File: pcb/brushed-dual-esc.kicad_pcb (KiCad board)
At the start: 2 copper layers, 29.5 x 25 mm, 33 parts, among them J1 XT30PW-M, J2 TC2030-NL, J3 Conn_02x03_Odd_Even, J4 XT30PW-F, J5 XT30PW-F, U1 AZ1117-5.0, U2 TLV77133PDBVR, U3 STM32C011F4Ux, U4 DRV8231ADSGR, U5 DRV8231ADSGR

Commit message: Start layout
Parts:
- removed D1: B1911USD, LED_SMD:LED_0603_1608Metric
- removed G***: LOGO, LOGO
- removed J1: XT30PW-M, Connector_AMASS:AMASS_XT30PW-M_1x02_P2.50mm_Horizontal
- removed R1: 270, Resistor_SMD:R_0603_1608Metric
- removed TP1: 5V, TestPoint:TestPoint_Pad_D2.0mm
- removed TP2: 3V3, TestPoint:TestPoint_Pad_D1.5mm
- removed U4, U5: DRV8231ADSGR, Package_SON:WSON-8-1EP_2x2mm_P0.5mm_EP0.9x1.6mm
- removed kibuzzard-68AF2469 (x2): G***, kibuzzard-68AF2469
- added D2: B1911USD, LED_SMD:LED_0603_1608Metric, F.Cu at (109.3, 106.0)
- added H1: M2, MountingHole:MountingHole_2.2mm_M2, F.Cu at (147.5, 52.5)
- added H2: M2, MountingHole:MountingHole_2.2mm_M2, F.Cu at (172.5, 72.5)
- added J6: DRV2_OUT1, Connector_Wire:SolderWirePad_1x01_SMD_2x4mm, F.Cu at (151.5, 72.5)
- added J7: DRV2_OUT2, Connector_Wire:SolderWirePad_1x01_SMD_2x4mm, F.Cu at (154.5, 72.5)
- added J8: +BATT, Connector_Wire:SolderWirePad_1x01_SMD_2x4mm, F.Cu at (172.5, 54.5)
- added J9: -BATT, Connector_Wire:SolderWirePad_1x01_SMD_2x4mm, F.Cu at (172.5, 59.5)
- added R6: 270, Resistor_SMD:R_0603_1608Metric, F.Cu at (106.0, 106.0)
- added U6: DRV8231ADDAR, Package_SO:Texas_HSOP-8-1EP_3.9x4.9mm_P1.27mm, F.Cu at (166.0, 66.0)
- added U7: DRV8231ADDAR, Package_SO:Texas_HSOP-8-1EP_3.9x4.9mm_P1.27mm, F.Cu at (153.0, 66.0)
- C1, C3: value 22u 16V -> CL21A226KOQNNNG; footprint Capacitor_SMD:C_0805_2012Metric -> Capacitor_SMD:C_1206_3216Metric
- C5: value ESS107M016AC2KA -> A750EM337M1CAAE015; footprint Capacitor_THT:CP_Radial_D5.0mm_P2.00mm -> Capacitor_THT:C_Radial_D6.3mm_H11.0mm_P2.50mm; moved to F.Cu
- J3: value Conn_02x03_Odd_Even -> DRV1_OUT1; footprint Connector_PinHeader_2.54mm:PinHeader_2x03_P2.54mm_Horizontal -> Connector_Wire:SolderWirePad_1x01_SMD_2x4mm; moved to F.Cu
- J4: value XT30PW-F -> Conn_01x04_Pin; footprint Connector_AMASS:AMASS_XT30PW-F_1x02_P2.50mm_Horizontal -> Connector_PinHeader_2.54mm:PinHeader_1x04_P2.54mm_Vertical; moved to F.Cu
- J5: value XT30PW-F -> DRV1_OUT2; footprint Connector_AMASS:AMASS_XT30PW-F_1x02_P2.50mm_Horizontal -> Connector_Wire:SolderWirePad_1x01_SMD_2x4mm; moved to F.Cu
- R2: value 30k -> 47k
- U1: value AZ1117-5.0 -> AZ1117CH-5.0TRG1
- U3: value STM32C011F4Ux -> STM32C011F6U6
- moved R4 49.0 mm to (173.3, 90.9), turned to 0 degrees
- moved C5 46.6 mm to (133.8, 142.5)
- moved C1 45.9 mm to (171.0, 51.5)
- moved J4 42.6 mm to (147.5, 57.7)
- moved C9 41.2 mm to (169.3, 88.4), turned to 0 degrees
- moved J3 40.7 mm to (164.5, 72.5), turned to 0 degrees
- moved R5 39.5 mm to (155.0, 60.5)
- moved C11 38.8 mm to (169.3, 93.4), turned to 0 degrees
- moved R3 38.6 mm to (96.1, 77.8)
- moved R2 37.8 mm to (96.2, 80.5), turned to 0 degrees
- moved C4 36.6 mm to (153.5, 52.0)
- moved U2 36.3 mm to (156.5, 52.0)
- moved C2 35.9 mm to (159.5, 52.0)
- moved C3 35.1 mm to (165.0, 51.5), turned to 0 degrees
- moved J5 34.6 mm to (167.5, 72.5)
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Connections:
- J3 pad 1: /RX_CH2 -> /DRV1_OUT1
- J4 pad 1: /DRV1_OUT2 -> /RX_CH2
- J4 pad 2: /DRV1_OUT1 -> /RX_CH1
- J5 pad 1: /DRV2_OUT2 -> /DRV1_OUT2
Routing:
- net +3V3: track 73.9 -> 0.00 mm, vias 2 -> 0
- net /DRV2_IN1: track 21.6 -> 0.00 mm, vias 4 -> 0
- net /DRV1_IN1: track 20.6 -> 0.00 mm, vias 2 -> 0
- net /DRV1_IN2: track 20.0 -> 0.00 mm
- net /DRV2_IN2: track 19.8 -> 0.00 mm, vias 4 -> 0
- net /DRV2_ISENSE: track 18.9 -> 0.00 mm, vias 4 -> 0
- net /DRV1_ISENSE: track 15.7 -> 0.00 mm, vias 2 -> 0
- net /RX_CH1: track 12.7 -> 0.00 mm, vias 1 -> 0
- net /RX_CH2: track 11.1 -> 0.00 mm, vias 1 -> 0
- net /~{RESET}: track 11.1 -> 0.00 mm, vias 4 -> 0
- net GND: track 8.17 -> 0.00 mm, vias 36 -> 0
- net /SWDIO: track 4.36 -> 0.00 mm
- net /BATT_SENSE: track 4.25 -> 0.00 mm
- net /SWCLK: track 4.05 -> 0.00 mm
- net Net-(D1-A): track 2.58 -> 0.00 mm
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- removed copper zone on F.Cu, net +3V3
- removed copper zone on F.Cu, net +5V
- removed copper zone on F.Cu, net +BATT
- removed copper zone on F.Cu, net /DRV1_OUT1
- removed copper zone on F.Cu, net /DRV1_OUT2
- removed copper zone on F.Cu, net /DRV2_OUT1
- removed copper zone on F.Cu, net /DRV2_OUT2
- removed copper zone on B.Cu, net GND
- removed copper zone on F.Cu, net GND
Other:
- board size 29.5 x 25 mm -> 30 x 25 mm
- board text removed: "3V3"
- board text removed: "5V 1A"
- board text removed: "CH1"
- board text removed: "CH2"
- board text removed: "Clarkson"
- board text removed: "Combat Robotics"
- board text removed: "Designed by Sigmond Kukla in 2025"
- board text removed: "GND"
- board text removed: "JLCJLCJLCJLC"
- board text removed: "SIG"
- board text removed: "University"

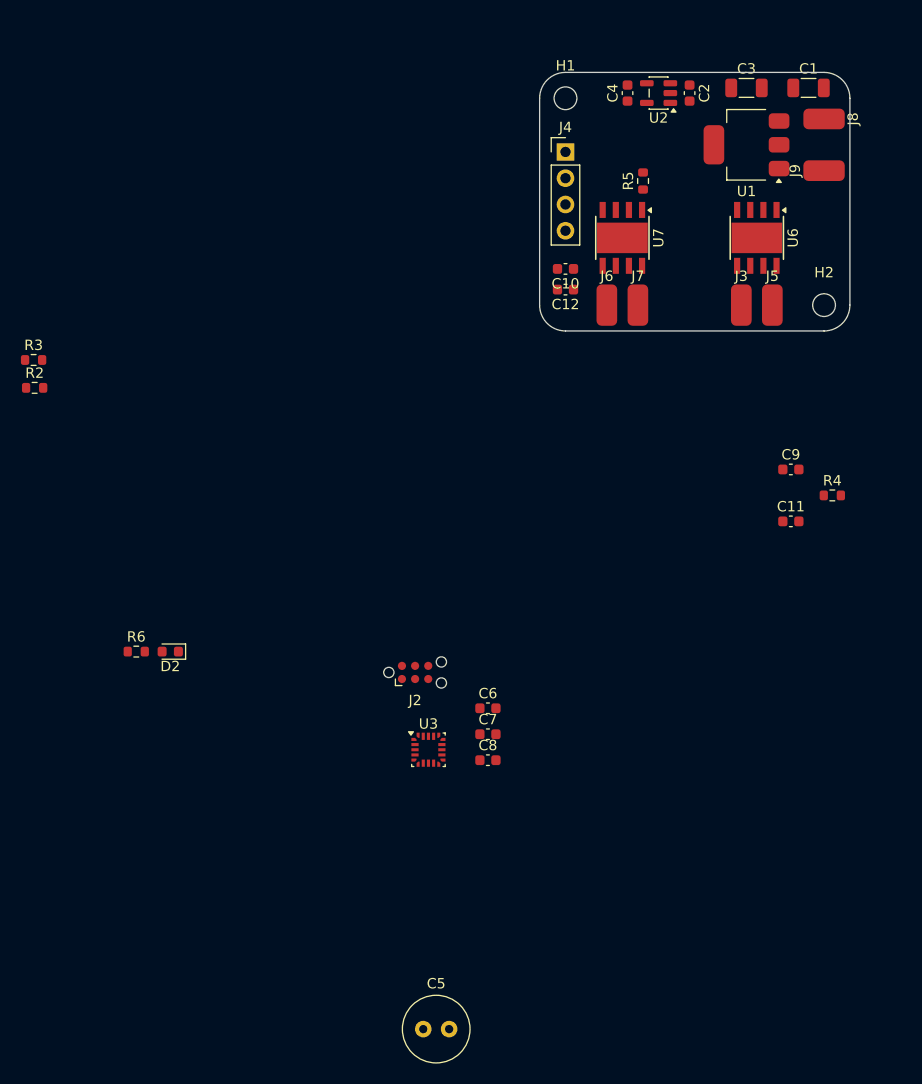
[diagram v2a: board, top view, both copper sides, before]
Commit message: Fit everything on the board
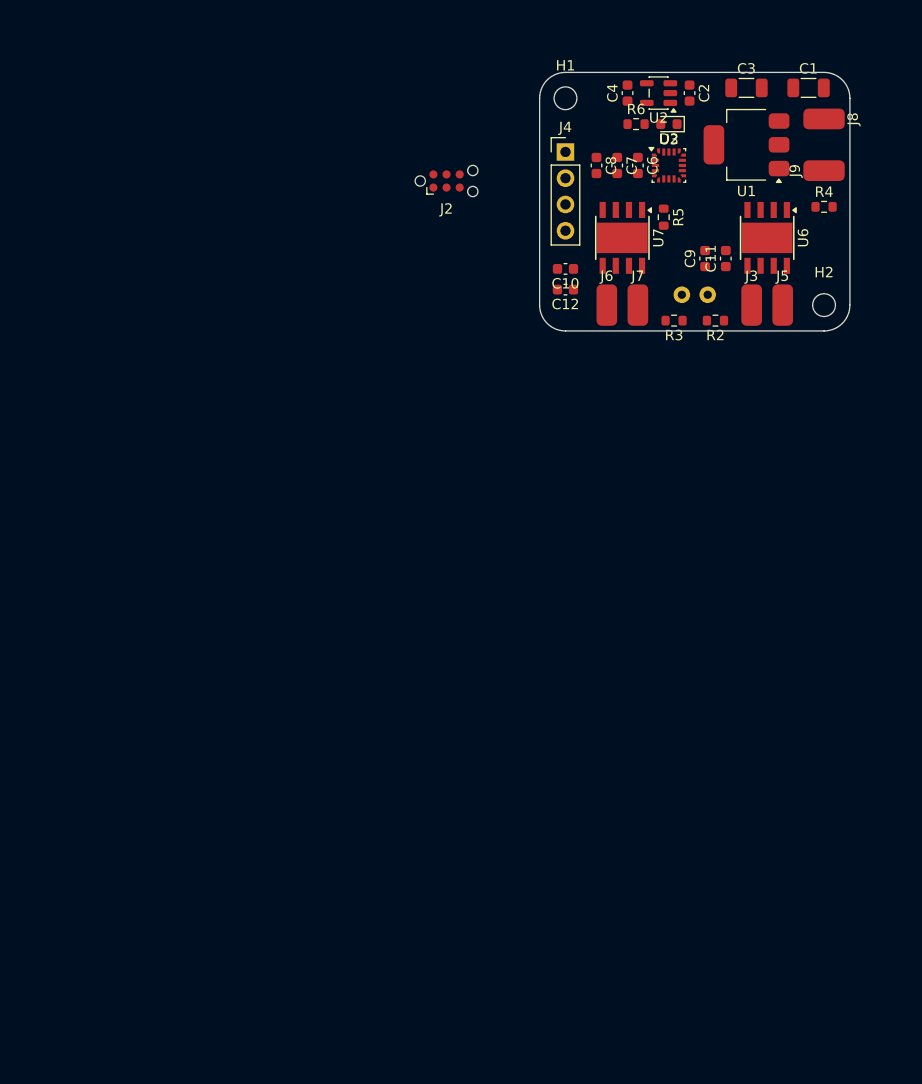
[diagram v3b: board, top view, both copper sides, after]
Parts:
- C5: moved to B.Cu
- moved C5 76.1 mm to (161.2, 71.5), turned to 180 degrees
- moved R6 70.3 mm to (154.3, 55.0)
- moved D2 70.2 mm to (157.5, 55.0)
- moved R2 66.1 mm to (162.0, 74.0), turned to 180 degrees
- moved R3 62.0 mm to (158.0, 74.0), turned to 180 degrees
- moved U3 61.1 mm to (157.5, 59.0)
- moved C8 58.5 mm to (150.5, 59.0), turned to -90 degrees
- moved C7 56.4 mm to (152.5, 59.0), turned to -90 degrees
- moved C6 54.4 mm to (154.5, 59.0), turned to -90 degrees
- moved J2 47.6 mm to (136.0, 60.5)
- moved R4 27.9 mm to (172.5, 63.0)
- moved C11 26.2 mm to (163.0, 68.0), turned to 90 degrees
- moved C9 22.0 mm to (161.0, 68.0), turned to 90 degrees
- moved R5 4.03 mm to (157.0, 64.0), turned to -90 degrees
- moved J3 1.00 mm to (165.5, 72.5)
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
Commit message: New layout
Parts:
- removed C12, C7: UMK107BJ105KA-T, Capacitor_SMD:C_0603_1608Metric
- C1, C3: value CL21A226KOQNNNG -> CL31A226KAHNNNE
- C10, C11: value UMK107BJ105KA-T -> A768EB107M1ELAS036; footprint Capacitor_SMD:C_0603_1608Metric -> Capacitor_SMD:CP_Elec_6.3x5.7
- C2, C4: value UMK107BJ105KA-T -> 4.7u
- C5: value A750EM337M1CAAE015 -> 4.7u; footprint Capacitor_THT:C_Radial_D6.3mm_H11.0mm_P2.50mm -> Capacitor_SMD:C_0603_1608Metric; moved to F.Cu
- C6, C8, C9: value UMK107BJ105KA-T -> 100n
- U1: value AZ1117CH-5.0TRG1 -> AZ1117CR-5.0TRG1; footprint Package_TO_SOT_SMD:SOT-223-3_TabPin2 -> Package_TO_SOT_SMD:SOT-89-3
- moved J5 23.7 mm to (147.5, 61.5), turned to -90 degrees
- moved J3 22.8 mm to (147.5, 58.5), turned to -90 degrees
- moved C4 22.1 mm to (156.0, 74.0), turned to 0 degrees
- moved J6 21.8 mm to (172.5, 66.5), turned to 90 degrees
- moved J7 20.1 mm to (172.5, 63.5), turned to 90 degrees
- moved R6 19.1 mm to (152.5, 74.0), turned to 180 degrees
- moved D2 17.7 mm to (152.5, 72.0)
- moved R3 17.4 mm to (169.5, 61.0)
- moved C10 17.2 mm to (155.0, 53.5), turned to 0 degrees
- moved R2 17.0 mm to (173.0, 61.0)
- moved J2 16.6 mm to (152.0, 64.9), turned to 180 degrees
- moved J4 15.8 mm to (146.5, 73.5), turned to 180 degrees
- moved C5 15.8 mm to (169.5, 58.0), turned to -90 degrees
- moved R4 15.6 mm to (157.0, 64.5), turned to -90 degrees
- moved U6 14.3 mm to (154.0, 60.0), turned to 180 degrees
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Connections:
- C5 pad 1: +BATT -> +3V3
- C8 pad 1: +3V3 -> +BATT
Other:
- outline, holes or cut-outs redrawn

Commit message: Begin routing
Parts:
- removed J4: Conn_01x04_Pin, Connector_PinHeader_2.54mm:PinHeader_1x04_P2.54mm_Vertical
- added J10: RX_CH2, Connector_Wire:SolderWirePad_1x01_SMD_1x2mm, F.Cu at (146.0, 73.5)
- added J11: RX_CH1, Connector_Wire:SolderWirePad_1x01_SMD_1x2mm, F.Cu at (148.5, 73.5)
- added J12: +5V, Connector_Wire:SolderWirePad_1x01_SMD_1x2mm, F.Cu at (151.0, 73.5)
- added J13: GND, Connector_Wire:SolderWirePad_1x01_SMD_1x2mm, F.Cu at (153.5, 73.5)
- moved R2 27.2 mm to (147.0, 69.0), turned to 0 degrees
- moved R3 20.6 mm to (150.5, 69.0), turned to 0 degrees
- moved C5 16.8 mm to (162.0, 73.0), turned to 90 degrees
- moved C2 16.0 mm to (169.0, 73.0), turned to 90 degrees
- moved U2 15.0 mm to (165.5, 73.0), turned to 180 degrees
- moved R6 5.10 mm to (157.5, 73.0), turned to -90 degrees
- moved C11 5.00 mm to (168.0, 67.5)
- moved C9 5.00 mm to (173.5, 65.0), turned to -90 degrees
- moved J7 5.00 mm to (172.5, 58.5)
- moved C4 4.61 mm to (159.0, 70.5)
- moved C6 4.61 mm to (159.0, 68.5)
- moved U3 4.61 mm to (159.0, 65.5)
- moved J6 4.50 mm to (172.5, 62.0)
- moved U7 4.50 mm to (166.0, 60.5)
- moved R5 4.00 mm to (164.0, 57.0)
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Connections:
- U3 pad 13: /DRV2_IN2 -> /DRV1_IN1
- U3 pad 14: /DRV2_IN1 -> /DRV1_IN2
- U3 pad 15: /BATT_SENSE -> /DRV1_ISENSE
- U3 pad 5: /DRV1_ISENSE -> /BATT_SENSE
- U3 pad 6: /DRV1_IN1 -> /DRV2_IN1
- U3 pad 7: /DRV1_IN2 -> /DRV2_IN2
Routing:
- net +3V3: track 0.00 -> 33.6 mm, vias 0 -> 3
- net +BATT: track 0.00 -> 31.3 mm, vias 0 -> 39
- net /BATT_SENSE: track 0.00 -> 21.2 mm, vias 0 -> 2
- net +5V: track 0.00 -> 17.5 mm, vias 0 -> 8
- net /RX_CH2: track 0.00 -> 15.9 mm
- net GND: track 0.00 -> 15.6 mm, vias 0 -> 25
- net /~{RESET}: track 0.00 -> 13.5 mm, vias 0 -> 2
- net /RX_CH1: track 0.00 -> 13.2 mm
- net /SWCLK: track 0.00 -> 10.4 mm
- net /DRV2_ISENSE: track 0.00 -> 9.76 mm
- net /SWDIO: track 0.00 -> 8.77 mm
- net /DRV2_IN2: track 0.00 -> 8.73 mm
- net /DRV2_IN1: track 0.00 -> 7.45 mm
- net /LED: track 0.00 -> 6.27 mm
- net /DRV1_IN1: track 0.00 -> 5.97 mm
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- added copper zone on B.Cu, net +5V
- added copper zone on F.Cu, net +5V
- added copper zone on B.Cu, net +BATT
- added copper zone on F.Cu, net +BATT
- added copper zone on F.Cu, net /DRV1_OUT1
- added copper zone on F.Cu, net /DRV1_OUT2
- added copper zone on F.Cu, net /DRV2_OUT1
- added copper zone on F.Cu, net /DRV2_OUT2
- added copper zone on B.Cu, net GND
- added copper zone on F.Cu, net GND

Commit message: Finish this diabolical routing
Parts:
- moved R2 15.8 mm to (162.8, 69.0), turned to 180 degrees
- moved R3 12.4 mm to (162.8, 70.6)
- moved C9 3.04 mm to (174.0, 68.0)
- moved C11 0.50 mm to (168.0, 67.0)
- moved C8 0.40 mm to (149.9, 56.0)
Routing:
- net +BATT: track 31.3 -> 4.71 mm, vias 39 -> 30
- net /BATT_SENSE: track 21.2 -> 4.44 mm, vias 2 -> 0
- net +3V3: track 33.6 -> 47.9 mm, vias 3 -> 6
- net +5V: track 17.5 -> 3.32 mm, vias 8 -> 10
- net Net-(D2-A): track 0.00 -> 2.02 mm
- net /RX_CH1: track 13.2 -> 15.1 mm
- net /RX_CH2: track 15.9 -> 17.7 mm
- net GND: track 15.6 -> 17.0 mm, vias 25 -> 41

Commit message: Cleanup spacing
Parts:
- moved R4 0.20 mm to (154.0, 64.3)
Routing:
- net GND: track 17.0 -> 17.7 mm, vias 41 -> 43
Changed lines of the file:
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@@
 	(footprint "Resistor_SMD:R_0603_1608Metric"
 		(layer "F.Cu")
-		(at 154 64.5 180)
+		(at 154 64.3 180)
 		(descr "Resistor SMD 0603 (1608 Metric), square (rectangular) end terminal, IPC-7351 nominal, (Body size source: IPC-SM-782 page 72, https://www.pcb-3d.com/wordpress/wp-content/uploads/ipc-sm-782a_amendment_1_and_2.pdf)")
 		(tags "resistor")
@@
 	)
 	(segment
+		(start 160.5 70.5)
+		(end 159.775 70.5)
+		(width 0.5)
+		(layer "F.Cu")
+		(net "GND")
+	)
+	(segment
 		(start 153.4 61.1)
 		(end 154 60.5)
@@
 	)
 	(segment
+		(start 159.775 68.5)
+		(end 160.275 69)
+		(width 0.5)
+		(layer "F.Cu")
+		(net "GND")
+	)
+	(segment
 		(start 152.3 61.1)
 		(end 153.4 61.1)
@@
 	)
 	(segment
-		(start 159.775 70.5)
-		(end 160 70.5)
-		(width 0.5)
-		(layer "F.Cu")
-		(net "GND")
-	)
-	(segment
-		(start 159.775 68.5)
-		(end 160.5 68.5)
+		(start 160.275 69)
+		(end 160.5 69)
 		(width 0.5)
 		(layer "F.Cu")
@@
 	)
 	(segment
-		(start 160 70.5)
-		(end 160.5 70)
-		(width 0.5)
-		(layer "F.Cu")
-		(net "GND")
-	)
-	(segment
 		(start 162.825 72.225)
 		(end 163 72.05)
@@
 	)
 	(segment
+		(start 153.175001 64.299999)
+		(end 152.5 64.3)
+		(width 0.3)
+		(layer "F.Cu")
+		(net "GND")
+	)
+	(segment
 		(start 153.5 72)
 		(end 153.5 73.5)
@@
 	)
 	(via
-		(at 160.5 70)
+		(at 160.5 70.5)
 		(size 0.6)
 		(drill 0.3)
@@
 	)
 	(via
+		(at 152.5 64.3)
+		(size 0.6)
+		(drill 0.3)
+		(layers "F.Cu" "B.Cu")
+		(net "GND")
+	)
+	(via
 		(at 156 56.5)
 		(size 0.6)
@@
 	)
 	(via
-		(at 160.5 68.5)
+		(at 160.5 69)
 		(size 0.6)
 		(drill 0.3)
@@
 	)
 	(via
+		(at 153.7 63.4)
+		(size 0.6)
+		(drill 0.3)
+		(layers "F.Cu" "B.Cu")
+		(net "GND")
+	)
+	(via
 		(at 157 57.5)
 		(size 0.6)
@@
 	)
 	(segment
-		(start 159.6 67.4)
-		(end 161.7 67.4)
+		(start 158.225 69.5)
+		(end 160.325 67.4)
 		(width 0.5)
 		(layer "B.Cu")
@@
 	)
 	(segment
-		(start 158.225 69.5)
-		(end 158.225 68.775)
-		(width 0.5)
-		(layer "B.Cu")
-		(net "+3V3")
-	)
-	(segment
-		(start 150.2 64.3)
-		(end 151 63.5)
+		(start 160.325 67.4)
+		(end 161.7 67.4)
 		(width 0.5)
 		(layer "B.Cu")
@@
 	)
 	(segment
-		(start 151 63.5)
-		(end 152.9 63.5)
+		(start 154.1 62.3)
+		(end 157.8 58.6)
 		(width 0.5)
 		(layer "B.Cu")
@@
 	)
 	(segment
-		(start 158.225 68.775)
-		(end 159.6 67.4)
+		(start 150.2 64.3)
+		(end 152.2 62.3)
 		(width 0.5)
 		(layer "B.Cu")
@@
 	)
 	(segment
-		(start 152.9 63.5)
-		(end 157.8 58.6)
+		(start 152.2 62.3)
+		(end 154.1 62.3)
 		(width 0.5)
 		(layer "B.Cu")
@@
 	)
 	(segment
-		(start 154.824999 64.280001)
-		(end 156.7 62.405)
+		(start 156.7 62.425)
+		(end 154.824999 64.300001)
 		(width 0.3)
 		(layer "F.Cu")
@@
 	)
 	(segment
-		(start 158 64.025)
-		(end 158 62.8)
+		(start 156.7 62.405)
+		(end 156.7 62.425)
 		(width 0.3)
 		(layer "F.Cu")
@@
 	)
 	(segment
-		(start 158 62.8)
-		(end 157.605 62.405)
+		(start 158 64.025)
+		(end 158 62.8)
 		(width 0.3)
 		(layer "F.Cu")
@@
 	)
 	(segment
-		(start 154.824999 64.500001)
-		(end 154.824999 64.280001)
+		(start 158 62.8)
+		(end 157.605 62.405)
 		(width 0.3)
 		(layer "F.Cu")
@@
 	)
 	(segment
+		(start 148.5 66.135)
+		(end 149.365 67)
+		(width 0.3)
+		(layer "F.Cu")
+		(net "/SWCLK")
+	)
+	(segment
 		(start 156.5 65)
 		(end 157.7 65)
@@
 		(width 0.3)
 		(layer "F.Cu")
-		(net "/SWCLK")
-	)
-	(segment
-		(start 148.5 66.135)
-		(end 149.365 67)
-		(width 0.3)
-		(layer "F.Cu")

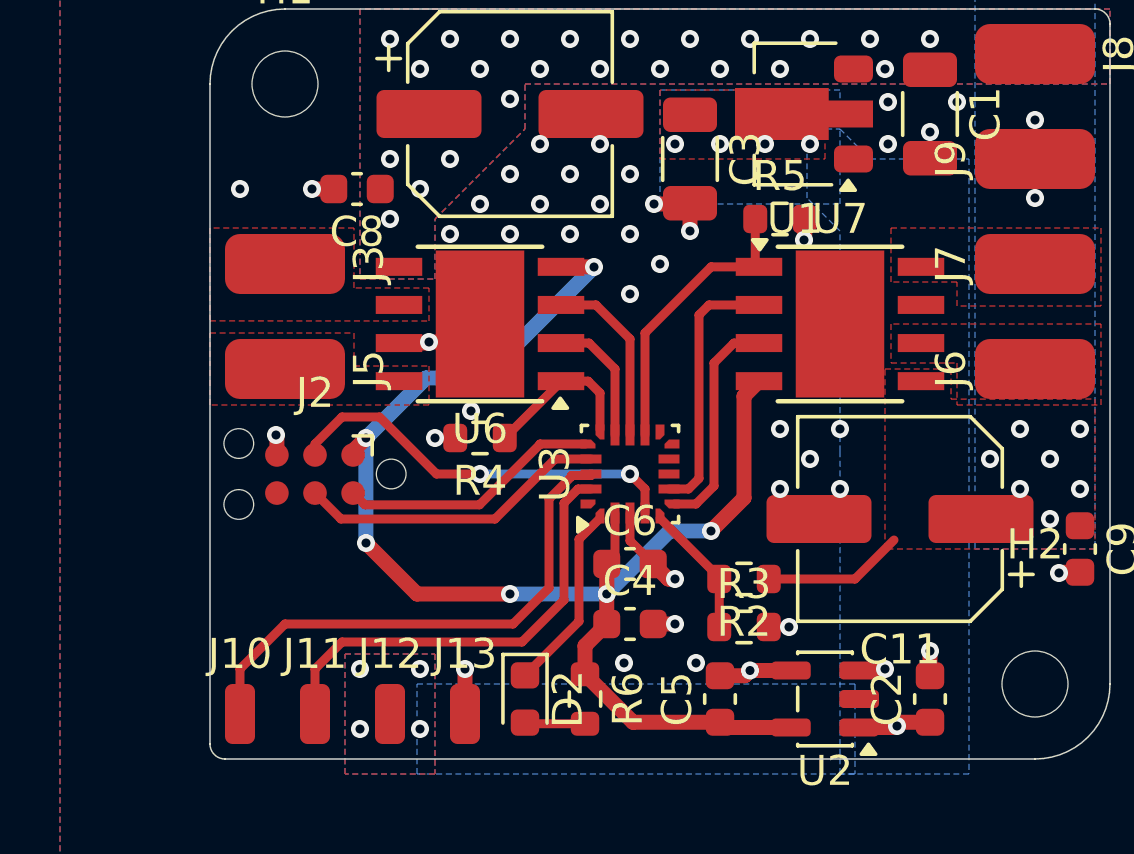
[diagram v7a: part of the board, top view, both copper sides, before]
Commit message: Cleanup routing
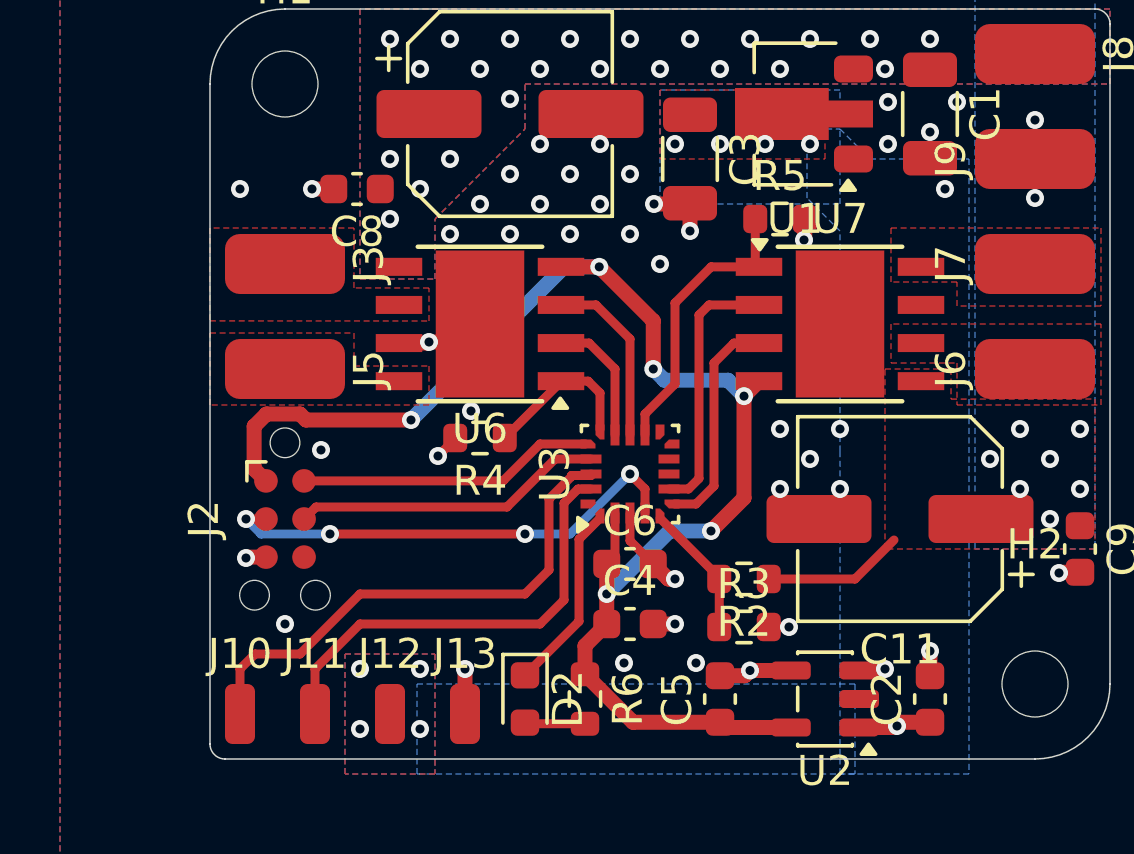
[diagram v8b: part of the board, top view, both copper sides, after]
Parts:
- moved J2 1.80 mm to (147.5, 67.0), turned to -90 degrees
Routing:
- net /~{RESET}: track 13.5 -> 16.0 mm, vias 2 -> 4
- net /SWDIO: track 8.77 -> 9.90 mm
- net +3V3: track 47.4 -> 48.1 mm
- net GND: track 17.7 -> 17.9 mm, vias 43 -> 45
